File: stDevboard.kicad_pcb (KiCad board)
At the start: 4 copper layers, 50 x 50 mm, 73 parts, among them IC1 MPM3610GQV-Z, IC2 MMC5603NJ, IC3 ICM-42670-P, IC4 MAX-F10S-00B, IC5 ICM-45686, IC6 KTS1622EUAA-TR, J9 USB_C_Receptacle_USB2.0_16P, Q1 IRLML6402, Q10 IRLML6244, Q11 IRLML6402, Q12 IRLML6244, Q2 IRLML6244, Q3 IRLML6402, Q4 IRLML6244, Q5 IRLML6402, Q6 IRLML6244, Q7 IRLML6402, Q8 IRLML6244, Q9 IRLML6402, U1 STM32, U2 BMP581

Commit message: pcb coming along, schematic way more done - I now have a lot more respect for hardware people than I did earlier
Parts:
- added D2: D, Diode_SMD:D_0402_1005Metric, F.Cu at (35.5, 40.4)
- added J1: antenna, Connector_Coaxial:U.FL_Molex_MCRF_73412-0110_Vertical, F.Cu at (159.2, 128.1)
- added J8: battery, Connector_PinHeader_2.54mm:PinHeader_1x02_P2.54mm_Vertical, F.Cu at (161.8, 94.1)
- added R25: 100, Resistor_SMD:R_0805_2012Metric, F.Cu at (35.6, 34.7)
- C20, C21, C22: moved to B.Cu
- U1: value STM32 -> STM32U585CIUxQ
- moved IC6 136.5 mm to (21.9, 48.4)
- moved Q12 125.2 mm to (32.7, 27.6)
- moved Q6 125.2 mm to (22.8, 27.6)
- moved Q9 125.2 mm to (27.8, 27.6)
- moved Q1 125.2 mm to (17.9, 18.6)
- moved Q10 125.2 mm to (32.7, 18.6)
- moved Q11 125.2 mm to (32.7, 23.1)
- moved Q2 125.2 mm to (17.9, 23.1)
- moved Q3 125.2 mm to (17.9, 27.6)
- moved Q4 125.2 mm to (22.8, 18.6)
- moved Q5 125.2 mm to (22.8, 23.1)
- moved Q7 125.2 mm to (27.8, 18.6)
- moved Q8 125.2 mm to (27.8, 23.1)
- moved R10 122.1 mm to (18.0, 33.8)
- moved R11 122.1 mm to (18.0, 35.6)
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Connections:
- Q1 pad 3: Net-(J2-Pin_1) -> c1_test
- Q10 pad 3: Net-(J6-Pin_2) -> Net-(J2-Pin_2)
- Q11 pad 3: Net-(J7-Pin_1) -> c6_test
- Q12 pad 3: Net-(J7-Pin_2) -> Net-(J2-Pin_2)
- Q3 pad 3: Net-(J3-Pin_1) -> c2_test
- Q4 pad 3: Net-(J3-Pin_2) -> Net-(J2-Pin_2)
- Q5 pad 3: Net-(J4-Pin_1) -> c3_test
- Q6 pad 3: Net-(J4-Pin_2) -> Net-(J2-Pin_2)
- Q7 pad 3: Net-(J5-Pin_1) -> c4_test
- Q8 pad 3: Net-(J5-Pin_2) -> Net-(J2-Pin_2)
- Q9 pad 3: Net-(J6-Pin_1) -> c5_test
- U1 pad 18: unconnected-(U1-PB0-Pad18) -> c1_test
- U1 pad 19: unconnected-(U1-PB1-Pad19) -> c2_test
- U1 pad 37: unconnected-(U1-PA14-Pad37) -> cont_test
- U1 pad 39: unconnected-(U1-PB3-Pad39) -> c3_test
- U1 pad 40: unconnected-(U1-PB4-Pad40) -> c4_test
- U1 pad 41: unconnected-(U1-PB5-Pad41) -> c5_test
- U1 pad 42: unconnected-(U1-PB6-Pad42) -> c6_test
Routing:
- net +3.3V: track 0.00 -> 113.4 mm, vias 0 -> 17
- net GND: track 13.0 -> 126.0 mm, vias 0 -> 21
- net i2c1_sda: track 0.00 -> 50.0 mm, vias 0 -> 3
- net i2c1_sck: track 0.00 -> 49.3 mm, vias 0 -> 6
- net UART_MISO: track 0.00 -> 34.8 mm, vias 0 -> 2
- net RST: track 0.00 -> 33.6 mm, vias 0 -> 2
- net UART_MOSI: track 0.00 -> 32.8 mm, vias 0 -> 3
- net GPS_PULSE: track 0.00 -> 29.9 mm
- net USB_D-: track 0.00 -> 25.9 mm, vias 0 -> 2
- net USB_D+: track 0.00 -> 25.1 mm
- net bmp_int: track 0.00 -> 24.2 mm, vias 0 -> 2
- net lowrate_lowg_int2: track 0.00 -> 21.1 mm, vias 0 -> 3
- net Net-(C8-Pad1): track 4.33 -> 21.7 mm, vias 0 -> 2
- net highrate_highg_int1: track 0.00 -> 16.2 mm, vias 0 -> 2
- net Net-(J9-CC2): track 0.00 -> 13.9 mm, vias 0 -> 1
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- added copper zone on In2.Cu, net +3.3V
- added copper zone on B.Cu, net +5V
- added copper zone on F.Cu, net GND
- added copper zone on In1.Cu, net GND

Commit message: tons of progress on schematic and pcb - see journal for details
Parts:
- removed IC6: KTS1622EUAA-TR, footprints:KTS1622EUAA-TR
- removed J8: battery, Connector_PinHeader_2.54mm:PinHeader_1x02_P2.54mm_Vertical
- removed J9: USB_C_Receptacle_USB2.0_16P, Connector_USB:USB_C_Receptacle_GCT_USB4085
- removed Q10, Q12, Q8: IRLML6244, Package_TO_SOT_SMD:SOT-23
- removed Q11, Q7, Q9: IRLML6402, Package_TO_SOT_SMD:SOT-23
- added BOOT1: Conn_01x02, Connector_PinHeader_2.54mm:PinHeader_1x02_P2.54mm_Vertical, F.Cu at (52.9, 58.9)
- added BOOT2: Conn_01x02, Connector_PinHeader_2.54mm:PinHeader_1x02_P2.54mm_Vertical, F.Cu at (73.0, 58.9)
- added C27: 7.5pF, Capacitor_SMD:C_0402_1005Metric, F.Cu at (26.7, 66.3)
- added C28: 3.9pF, Capacitor_SMD:C_0402_1005Metric, F.Cu at (26.7, 68.2)
- added C29: 1.8pF, Capacitor_SMD:C_0402_1005Metric, F.Cu at (26.7, 70.2)
- added C30: 22pF, Capacitor_SMD:C_0402_1005Metric, F.Cu at (26.7, 72.2)
- added C31: 1.8pF, Capacitor_SMD:C_0402_1005Metric, F.Cu at (29.6, 64.3)
- added C32: 2.2pF, Capacitor_SMD:C_0402_1005Metric, F.Cu at (29.6, 66.3)
- added C33: 18pF, Capacitor_SMD:C_0402_1005Metric, F.Cu at (29.6, 68.2)
- added C34: 1uF, Capacitor_SMD:C_0603_1608Metric, F.Cu at (20.4, 55.4)
- added C35: 1uF, Capacitor_SMD:C_0603_1608Metric, F.Cu at (20.4, 57.9)
- added C36: 100nF, Capacitor_SMD:C_0402_1005Metric, F.Cu at (29.6, 70.2)
- added C37: 2.2uF, Capacitor_SMD:C_0603_1608Metric, F.Cu at (20.4, 60.4)
- added C38: 4.7uF, Capacitor_SMD:C_0603_1608Metric, F.Cu at (20.4, 62.9)
- added C39: 10uF, Capacitor_SMD:C_0603_1608Metric, F.Cu at (20.4, 65.4)
- added C40: 0.1uF, Capacitor_SMD:C_0402_1005Metric, F.Cu at (29.6, 72.2)
- added C41: 10uF, Capacitor_SMD:C_0603_1608Metric, F.Cu at (84.8, 57.9)
- added C42: 100nF, Capacitor_SMD:C_0402_1005Metric, F.Cu at (69.3, 48.3)
- added C43: 1uF, Capacitor_SMD:C_0603_1608Metric, F.Cu at (84.8, 60.4)
- added C44: 100nF, Capacitor_SMD:C_0402_1005Metric, F.Cu at (69.3, 50.3)
- added C45: 100nF, Capacitor_SMD:C_0402_1005Metric, F.Cu at (69.3, 52.2)
- added C46: 100nF, Capacitor_SMD:C_0402_1005Metric, F.Cu at (69.3, 54.2)
- added C47: 100nF, Capacitor_SMD:C_0402_1005Metric, F.Cu at (69.3, 56.2)
- added C48: 9pF, Capacitor_SMD:C_0402_1005Metric, F.Cu at (69.3, 58.2)
- added C49: 9pF, Capacitor_SMD:C_0402_1005Metric, F.Cu at (69.3, 60.1)
- added D3: D, Diode_SMD:D_0603_1608Metric, F.Cu at (29.3, 37.7)
- added D4: D_Schottky, Diode_SMD:D_0805_2012Metric, F.Cu at (133.3, 83.2)
- added FB1: BLM15AX102SN1D, footprints:NFZ15SG152SN10B, F.Cu at (123.8, 83.2)
- added FB2: BLM15AX102SN1D, footprints:NFZ15SG152SN10B, F.Cu at (126.2, 83.2)
- added J11: USB_C_Receptacle_USB2.0_16P, Connector_USB:USB_C_Receptacle_GCT_USB4085, F.Cu at (133.3, 81.0)
- added J12: Conn_01x06, Connector_PinHeader_2.54mm:PinHeader_1x06_P2.54mm_Vertical, F.Cu at (49.8, 91.2)
- added J2: USB_C_Receptacle_USB2.0_16P, Connector_USB:USB_C_Receptacle_GCT_USB4085, F.Cu at (122.7, 81.0)
- added J3: Conn_02x03_Top_Bottom, Connector_PinHeader_2.54mm:PinHeader_2x02_P2.54mm_Vertical, F.Cu at (92.7, 36.2)
- added L2: 12nH, Inductor_SMD:L_0402_1005Metric, F.Cu at (23.8, 52.6)
- added L3: 22nH, Inductor_SMD:L_0402_1005Metric, F.Cu at (23.8, 54.6)
- added L4: 4.7nH, Inductor_SMD:L_0402_1005Metric, F.Cu at (23.8, 56.6)
- added L5: 3.9nH, Inductor_SMD:L_0402_1005Metric, F.Cu at (23.8, 58.5)
- added L6: 7.5nH, Inductor_SMD:L_0402_1005Metric, F.Cu at (23.8, 60.5)
- added L7: 24nH, Inductor_SMD:L_0402_1005Metric, F.Cu at (23.8, 62.5)
- added L8: 2.2uH, Inductor_SMD:L_0402_1005Metric, F.Cu at (23.8, 64.5)
- added LR1: ~, footprints:Untitled, F.Cu at (31.8, 69.4)
- added R26: 10k, Resistor_SMD:R_0402_1005Metric, F.Cu at (81.4, 59.6)
- added R27: 10k, Resistor_SMD:R_0402_1005Metric, F.Cu at (81.4, 61.6)
- added R28: 10k, Resistor_SMD:R_0402_1005Metric, F.Cu at (81.4, 63.6)
- added RST1: Conn_01x02, Connector_PinHeader_2.54mm:PinHeader_1x02_P2.54mm_Vertical, F.Cu at (85.4, 92.6)
- added RST2: Conn_01x02, Connector_PinHeader_2.54mm:PinHeader_1x02_P2.54mm_Vertical, F.Cu at (77.6, 58.9)
- added U3: BMP581, footprints:BMP581, F.Cu at (125.0, 114.0)
- added U4: MAX-M10S, RF_GPS:ublox_MAX, F.Cu at (112.3, 159.6)
- added Y1: ECS-160-8-36B2-CKM-TR, footprints:ECS160836B2CKMTR, F.Cu at (106.2, 98.0)
- added Y2: CM7V-T1A-32.768KHZ, footprints:CM7V32768TBQA020, F.Cu at (105.2, 92.8)
- added Y3: ECS-TXO-25CSMV-320-AM-TR, footprints:ECSTXO25CSMV320AMTR, F.Cu at (34.0, 66.0)
- added Y4: CM7V-T1A-32.768KHZ, footprints:CM7V32768TBQA020, F.Cu at (83.7, 49.8)
- C1: value 22uF -> 10uF; footprint Capacitor_SMD:C_0603_1608Metric -> Capacitor_SMD:C_0805_2012Metric
- C10: value 1 uF -> 100 nF; footprint Capacitor_SMD:C_0603_1608Metric -> Capacitor_SMD:C_0402_1005Metric
- C12: value 10 uF -> 100 nF; footprint Capacitor_SMD:C_0603_1608Metric -> Capacitor_SMD:C_0402_1005Metric
- C13, C14: value 100 nF -> 2.2 uF; footprint Capacitor_SMD:C_0402_1005Metric -> Capacitor_SMD:C_0603_1608Metric
- C15: value 100 nF -> 1 uF; footprint Capacitor_SMD:C_0402_1005Metric -> Capacitor_SMD:C_0603_1608Metric
- C16: value 2.2uF -> 100 nF; footprint Capacitor_SMD:C_0603_1608Metric -> Capacitor_SMD:C_0402_1005Metric
- C17: value 0.1uF -> 10 uF; footprint Capacitor_SMD:C_0402_1005Metric -> Capacitor_SMD:C_0603_1608Metric; moved to B.Cu
- C18: value 10uF -> 100 nF; footprint Capacitor_SMD:C_0603_1608Metric -> Capacitor_SMD:C_0402_1005Metric; moved to B.Cu
- C19: value 0.1uf -> 100 nF
- C2: value 10uF -> 22uF
- C20: value 2.2uF -> 0.1uF; footprint Capacitor_SMD:C_0603_1608Metric -> Capacitor_SMD:C_0402_1005Metric; moved to F.Cu
- C21: moved to F.Cu
- C22: value 10nF -> 0.1uF; moved to F.Cu
- C23: value 10nF -> 0.1uF
- C24: value 2.2uF -> 10uF
- C25: value 0.1uF -> 2.2uF; footprint Capacitor_SMD:C_0402_1005Metric -> Capacitor_SMD:C_0603_1608Metric
- C26: value 100uF -> 47pF; footprint Capacitor_SMD:C_0805_2012Metric -> Capacitor_SMD:C_0402_1005Metric
- C3: value 10 uF -> 10uF
- C4: value 100 nF -> 8pF
- C5, C6: value 100 nF -> 9pF
- C7: value 1 uF -> 8pF; footprint Capacitor_SMD:C_0603_1608Metric -> Capacitor_SMD:C_0402_1005Metric
- C8: value 2.2 uF -> 1 uF
- C9: value 2.2 uF -> 10 uF
- D1: value D_Zener -> D; footprint Diode_SMD:D_0402_1005Metric -> Diode_SMD:D_0603_1608Metric
- D2: footprint Diode_SMD:D_0402_1005Metric -> Diode_SMD:D_0603_1608Metric
- IC2: value MMC5603NJ -> IRFR9014PBF; footprint footprints:MMC5603NJ -> footprints:TO228P990X238-3N
- IC3: value ICM-42670-P -> ICM-45686; moved to F.Cu
- IC4: value MAX-F10S-00B -> ICM-45686; footprint footprints:MAXF10S00B -> footprints:ICM42670P
- IC5: value ICM-45686 -> MMC5983MA; footprint footprints:ICM42670P -> footprints:MMC5983MA
- J1: value antenna -> battery; footprint Connector_Coaxial:U.FL_Molex_MCRF_73412-0110_Vertical -> Connector_PinHeader_2.54mm:PinHeader_1x02_P2.54mm_Vertical
- Q1, Q3, Q5: value IRLML6402 -> IRLML6244
- R1: value 100k -> 5.1K
- R10: value 100 -> 1k; footprint Resistor_SMD:R_0201_0603Metric -> Resistor_SMD:R_0402_1005Metric
- R11: value 100 -> 10k; footprint Resistor_SMD:R_0201_0603Metric -> Resistor_SMD:R_0402_1005Metric
- R12, R13: value 100 -> 2.7k; footprint Resistor_SMD:R_0201_0603Metric -> Resistor_SMD:R_0402_1005Metric
- R14: value 100 -> 1k; footprint Resistor_SMD:R_0201_0603Metric -> Resistor_SMD:R_0805_2012Metric
- R15: value 100 -> 10k; footprint Resistor_SMD:R_0201_0603Metric -> Resistor_SMD:R_0603_1608Metric
- R16, R17, R18, R19, R20, R21: footprint Resistor_SMD:R_0201_0603Metric -> Resistor_SMD:R_0603_1608Metric
- R22: value 39k -> 100; footprint Resistor_SMD:R_0201_0603Metric -> Resistor_SMD:R_0603_1608Metric
- R23: value 75k -> 5.1K; footprint Resistor_SMD:R_0201_0603Metric -> Resistor_SMD:R_0402_1005Metric
- R24: value 24k -> 5.1K; footprint Resistor_SMD:R_0201_0603Metric -> Resistor_SMD:R_0402_1005Metric
- R25: value 100 -> 1k; footprint Resistor_SMD:R_0805_2012Metric -> Resistor_SMD:R_0402_1005Metric
- R3: value 5.1K -> 75k; footprint Resistor_SMD:R_0402_1005Metric -> Resistor_SMD:R_0201_0603Metric
- R4: value 10k -> 24k; footprint Resistor_SMD:R_0402_1005Metric -> Resistor_SMD:R_0201_0603Metric
- R5: value 10k -> 39k; footprint Resistor_SMD:R_0402_1005Metric -> Resistor_SMD:R_0201_0603Metric
- R6: value 2.7k -> 100k
- R7, R8: value 2.7k -> 10k
- R9: value 2.7k -> 1k
- U1: value STM32U585CIUxQ -> STM32U073CCUx; footprint Package_DFN_QFN:QFN-48-1EP_7x7mm_P0.5mm_EP5.6x5.6mm -> Package_DFN_QFN:QFN-48-1EP_7x7mm_P0.5mm_EP5.6x5.6mm_ThermalVias
- U2: value BMP581 -> STM32U585CIUxQ; footprint footprints:BMP581 -> Package_DFN_QFN:QFN-48-1EP_7x7mm_P0.5mm_EP5.6x5.6mm_ThermalVias
- moved C25 164.9 mm to (20.4, 52.8)
- moved D1 160.9 mm to (29.3, 32.5), turned to 0 degrees
- moved R22 140.9 mm to (25.3, 41.7), turned to 0 degrees
- moved C9 137.1 mm to (48.6, 51.1), turned to 0 degrees
- moved R7 137.0 mm to (48.1, 63.4)
- moved R8 125.4 mm to (48.1, 65.4), turned to 0 degrees
- moved C23 125.3 mm to (77.5, 31.8)
- moved C22 125.0 mm to (77.5, 29.8), turned to 0 degrees
- moved C20 122.7 mm to (77.5, 25.8), turned to 0 degrees
- moved C21 120.7 mm to (77.5, 27.8), turned to 0 degrees
- moved C26 114.7 mm to (26.7, 64.3), turned to 0 degrees
- moved R10 111.3 mm to (110.1, 96.4)
- moved IC2 109.5 mm to (71.8, 71.0)
- moved C4 82.6 mm to (103.2, 97.9), turned to 90 degrees
- moved C8 78.0 mm to (108.8, 93.4), turned to -90 degrees
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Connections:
- C1 pad 1: GND -> +BATT
- C1 pad 2: +3.3V -> GND
- C12 pad 1: +3.3V -> GND
- C12 pad 2: GND -> +3.3V
- C13 pad 1: +3.3V -> Net-(C13-Pad1)
- C14 pad 1: GND -> Net-(C13-Pad1)
- C14 pad 2: Net-(D1-K) -> GND
- C19 pad 2: Net-(IC6-VDD_I2C) -> +3.3V
- C2 pad 1: +5V -> GND
- C2 pad 2: GND -> +3.3V
- C24 pad 1: +3.3V -> Net-(IC5-CAP)
- C25 pad 1: +3.3V -> GND
- C25 pad 2: GND -> +3.3V
- C26 pad 1: +5V -> vr_pa
- C3 pad 1: GND -> +BATT
- C3 pad 2: +3.3V -> GND
- C4 pad 1: GND -> Net-(Y1-OUT/IN)
- C4 pad 2: +3.3V -> Net-(Y1-GND_1)
- C5 pad 2: +3.3V -> Net-(C5-Pad2)
- C6 pad 1: GND -> Net-(U2-PC13)
- C6 pad 2: +3.3V -> GND
- C7 pad 1: GND -> Net-(U2-PH0)
- C7 pad 2: +3.3V -> Net-(Y1-GND_2)
- C8 pad 1: Net-(C8-Pad1) -> GND
- C9 pad 1: Net-(C8-Pad1) -> GND
- D1 pad 2: GND -> cont_test
- D2 pad 2: cont_test -> arm
- IC1 pad 16: +5V -> +BATT
- IC3 pad 4: lowrate_lowg_int1 -> imu1_int1
- IC3 pad 9: lowrate_lowg_int2 -> unconnected-(IC3-INT2-Pad9)
- IC4 pad 10: GND -> unconnected-(IC4-RESV_3-Pad10)
- IC4 pad 11: Net-(IC4-RF_IN) -> unconnected-(IC4-RESV_4-Pad11)
- IC4 pad 12: GND -> +3.3V
- IC4 pad 13: +3.3V -> i2c1_sck
- IC4 pad 14: +3.3V -> i2c1_sda
- IC4 pad 2: UART_MISO -> unconnected-(IC4-RESV_1-Pad2)
- IC4 pad 3: UART_MOSI -> unconnected-(IC4-RESV_2-Pad3)
- IC4 pad 4: GPS_PULSE -> imu2_int1
- IC4 pad 5: unconnected-(IC4-EXTINT-Pad5) -> +3.3V
- IC4 pad 6: +3.3V -> GND
- IC4 pad 7: +3.3V -> GND
- IC4 pad 9: RST -> unconnected-(IC4-INT2-Pad9)
- IC5 pad 1: +3.3V -> i2c1_sck
- IC5 pad 10: unconnected-(IC5-RESV_3-Pad10) -> Net-(IC5-CAP)
- IC5 pad 11: unconnected-(IC5-RESV_4-Pad11) -> GND
- IC5 pad 12: +3.3V -> unconnected-(IC5-NC_5-Pad12)
- IC5 pad 13: i2c1_sck -> +3.3V
- IC5 pad 14: i2c1_sda -> unconnected-(IC5-NC_6-Pad14)
- IC5 pad 2: unconnected-(IC5-RESV_1-Pad2) -> +3.3V
- IC5 pad 4: highrate_highg_int1 -> +3.3V
- IC5 pad 5: +3.3V -> unconnected-(IC5-SPI_SDO-Pad5)
- IC5 pad 6: GND -> unconnected-(IC5-NC_2-Pad6)
- IC5 pad 7: GND -> unconnected-(IC5-NC_3-Pad7)
- IC5 pad 8: +3.3V -> unconnected-(IC5-NC_4-Pad8)
- IC5 pad 9: highrate_highg_int2 -> GND
- J1 pad 1: Net-(IC4-RF_IN) -> GND
- J1 pad 2: GND -> +BATT
- L1 pad 1: Net-(U1-VLXSMPS) -> Net-(U2-VLXSMPS)
- L1 pad 2: Net-(C8-Pad1) -> Net-(C13-Pad1)
- Q1 pad 2: +5V -> GND
- Q1 pad 3: c1_test -> cont_test_out
- Q2 pad 3: Net-(J2-Pin_2) -> cont_test_out
- Q3 pad 2: +5V -> GND
- Q3 pad 3: c2_test -> cont_test_out
- Q4 pad 3: Net-(J2-Pin_2) -> cont_test_out
- Q5 pad 2: +5V -> GND
- Q5 pad 3: c3_test -> cont_test_out
- Q6 pad 3: Net-(J2-Pin_2) -> cont_test_out
- R1 pad 1: Net-(IC1-EN) -> Net-(J2-CC1)
- R1 pad 2: +5V -> GND
- R10 pad 1: Net-(Q2-G) -> Net-(C5-Pad2)
- R10 pad 2: c1_arm -> Net-(U2-PC14)
- R11 pad 1: Net-(Q1-G) -> Net-(RST1-Pin_2)
- R11 pad 2: c1_fire -> +3.3V
- R12 pad 1: Net-(Q3-G) -> i2c1_sda
- R12 pad 2: c2_fire -> +3.3V
- R13 pad 1: Net-(Q4-G) -> i2c1_sck
- R13 pad 2: c2_arm -> +3.3V
- R14 pad 1: Net-(Q5-G) -> cont_test_out
- R14 pad 2: c3_fire -> Net-(D1-K)
- R15 pad 1: Net-(Q6-G) -> Net-(D2-K)
- R15 pad 2: c3_arm -> +BATT
- R16 pad 1: Net-(Q7-G) -> Net-(Q1-G)
- R16 pad 2: c4_fire -> c1_fire
- R17 pad 1: Net-(Q8-G) -> cont_test_in
- R17 pad 2: c4_arm -> Net-(D3-K)
- R18 pad 1: Net-(Q9-G) -> Net-(Q2-G)
- R18 pad 2: c5_fire -> c2_fire
- R19 pad 1: Net-(Q10-G) -> Net-(Q3-G)
- R19 pad 2: c5_arm -> c3_fire
- R20 pad 1: Net-(Q11-G) -> Net-(Q4-G)
- R20 pad 2: c6_fire -> c4_fire
- R21 pad 1: Net-(Q12-G) -> Net-(Q5-G)
- R21 pad 2: c6_arm -> c5_fire
- R22 pad 1: Net-(IC1-AAM) -> Net-(Q6-G)
- R22 pad 2: GND -> c6_fire
- R23 pad 1: +3.3V -> Net-(J11-CC1)
- R23 pad 2: Net-(IC1-FB) -> GND
- R24 pad 1: Net-(IC1-FB) -> Net-(J11-CC2)
- R25 pad 1: Net-(J2-Pin_2) -> Net-(C48-Pad2)
- R25 pad 2: Net-(D2-K) -> Net-(U1-PC14)
- R3 pad 1: Net-(J9-CC2) -> +3.3V
- R3 pad 2: GND -> Net-(IC1-FB)
- R4 pad 1: Net-(BOOT1-Pad2) -> Net-(IC1-FB)
- R4 pad 2: Net-(U1-PH3) -> GND
- R5 pad 1: Net-(BOOT1-Pad2) -> Net-(IC1-AAM)
- R6 pad 1: Net-(IC2-SCL) -> Net-(IC1-EN)
- R6 pad 2: i2c1_sck -> +BATT
- R7 pad 1: Net-(IC2-SDA) -> GND
- R7 pad 2: i2c1_sda -> Net-(BOOT1-Pin_1)
- R8 pad 1: i2c1_sda -> Net-(BOOT1-Pin_1)
- R8 pad 2: +3.3V -> Net-(U2-PH3)
- R9 pad 1: i2c1_sck -> Net-(Y1-OUT/IN)
- R9 pad 2: +3.3V -> Net-(U2-PH1)
- U1 pad 10: UART_MOSI -> unconnected-(U1-PA0-Pad10)
- U1 pad 11: UART_MISO -> unconnected-(U1-PA1-Pad11)
- U1 pad 12: highrate_highg_int1 -> usart_mosi
- U1 pad 13: highrate_highg_int2 -> usart_miso
- U1 pad 14: lowrate_lowg_int1 -> usart_ck
- U1 pad 15: lowrate_lowg_int2 -> spi_sclk
- U1 pad 16: bmp_int -> spi_miso
- U1 pad 17: GPS_PULSE -> spi_mosi
- U1 pad 18: c1_test -> unconnected-(U1-PB0-Pad18)
- U1 pad 19: c2_test -> unconnected-(U1-PB1-Pad19)
- U1 pad 2: unconnected-(U1-PC13-Pad2) -> Net-(U1-PC13)
- U1 pad 20: Net-(U1-VLXSMPS) -> unconnected-(U1-PB2-Pad20)
- U1 pad 21: +3.3V -> unconnected-(U1-PB10-Pad21)
- U1 pad 22: GND -> unconnected-(U1-PB11-Pad22)
- U1 pad 23: Net-(C8-Pad1) -> GND
- U1 pad 24: GND -> +3.3V
- U1 pad 25: +3.3V -> unconnected-(U1-PB12-Pad25)
- U1 pad 3: unconnected-(U1-PC14-Pad3) -> Net-(U1-PC14)
- U1 pad 30: unconnected-(U1-PA9-Pad30) -> ppu_tx_external
- U1 pad 31: unconnected-(U1-PA10-Pad31) -> ppu_rx_external
- U1 pad 32: USB_D- -> USB2_D-
- U1 pad 33: USB_D+ -> USB2_D+
- U1 pad 37: cont_test -> telem_busy
- U1 pad 38: RST -> telem_rst
- U1 pad 39: c3_test -> unconnected-(U1-PB3-Pad39)
- U1 pad 40: c4_test -> unconnected-(U1-PB4-Pad40)
- U1 pad 41: c5_test -> unconnected-(U1-PB5-Pad41)
- U1 pad 42: c6_test -> unconnected-(U1-PB6-Pad42)
- U1 pad 43: i2c1_sda -> unconnected-(U1-PB7-Pad43)
- U1 pad 44: Net-(U1-PH3) -> Net-(U1-PF3)
- U1 pad 45: i2c1_sck -> unconnected-(U1-PB8-Pad45)
- U1 pad 46: Net-(C8-Pad1) -> unconnected-(U1-PB9-Pad46)
- U1 pad 7: Net-(D1-K) -> Net-(RST2-Pin_2)
- U2 pad 10: +3.3V -> /main micro/servo1
- U2 pad 2: i2c1_sck -> Net-(U2-PC13)
- U2 pad 3: GND -> Net-(U2-PC14)
- U2 pad 4: i2c1_sda -> unconnected-(U2-PC15-Pad4)
- U2 pad 5: GND -> Net-(U2-PH0)
- U2 pad 6: +3.3V -> Net-(U2-PH1)
- U2 pad 7: bmp_int -> Net-(RST1-Pin_2)
- U2 pad 9: GND -> +3.3V
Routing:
- net +3.3V: track 113.4 -> 43.6 mm, vias 17 -> 27
- net i2c1_sda: track 50.0 -> 0.00 mm, vias 3 -> 0
- net i2c1_sck: track 49.3 -> 5.55 mm, vias 6 -> 0
- net UART_MISO: track 34.8 -> 0.00 mm, vias 2 -> 0
- net RST: track 33.6 -> 0.00 mm, vias 2 -> 0
- net UART_MOSI: track 32.8 -> 0.00 mm, vias 3 -> 0
- net +BATT: track 0.00 -> 30.8 mm
- net GPS_PULSE: track 29.9 -> 0.00 mm
- net Net-(C13-Pad1): track 0.00 -> 26.4 mm, vias 0 -> 1
- net Net-(C8-Pad1): track 21.7 -> 0.00 mm, vias 2 -> 0
- net lowrate_lowg_int2: track 21.1 -> 0.00 mm, vias 3 -> 0
- net Net-(J2-SHIELD): track 0.00 -> 18.8 mm
- net Net-(J11-SHIELD): track 0.00 -> 18.8 mm
- net highrate_highg_int1: track 16.2 -> 0.00 mm, vias 2 -> 0
- net USB2_D-: track 0.00 -> 14.0 mm, vias 0 -> 1
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- added copper zone on In1.Cu, net +3.3V
- added copper zone on B.Cu, net GND
- added copper zone on In2.Cu, net GND
- removed copper zone on In2.Cu, net +3.3V
- removed copper zone on B.Cu, net +5V
- removed copper zone on In1.Cu, net GND
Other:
- board size 50 x 50 mm -> 50 x 100 mm

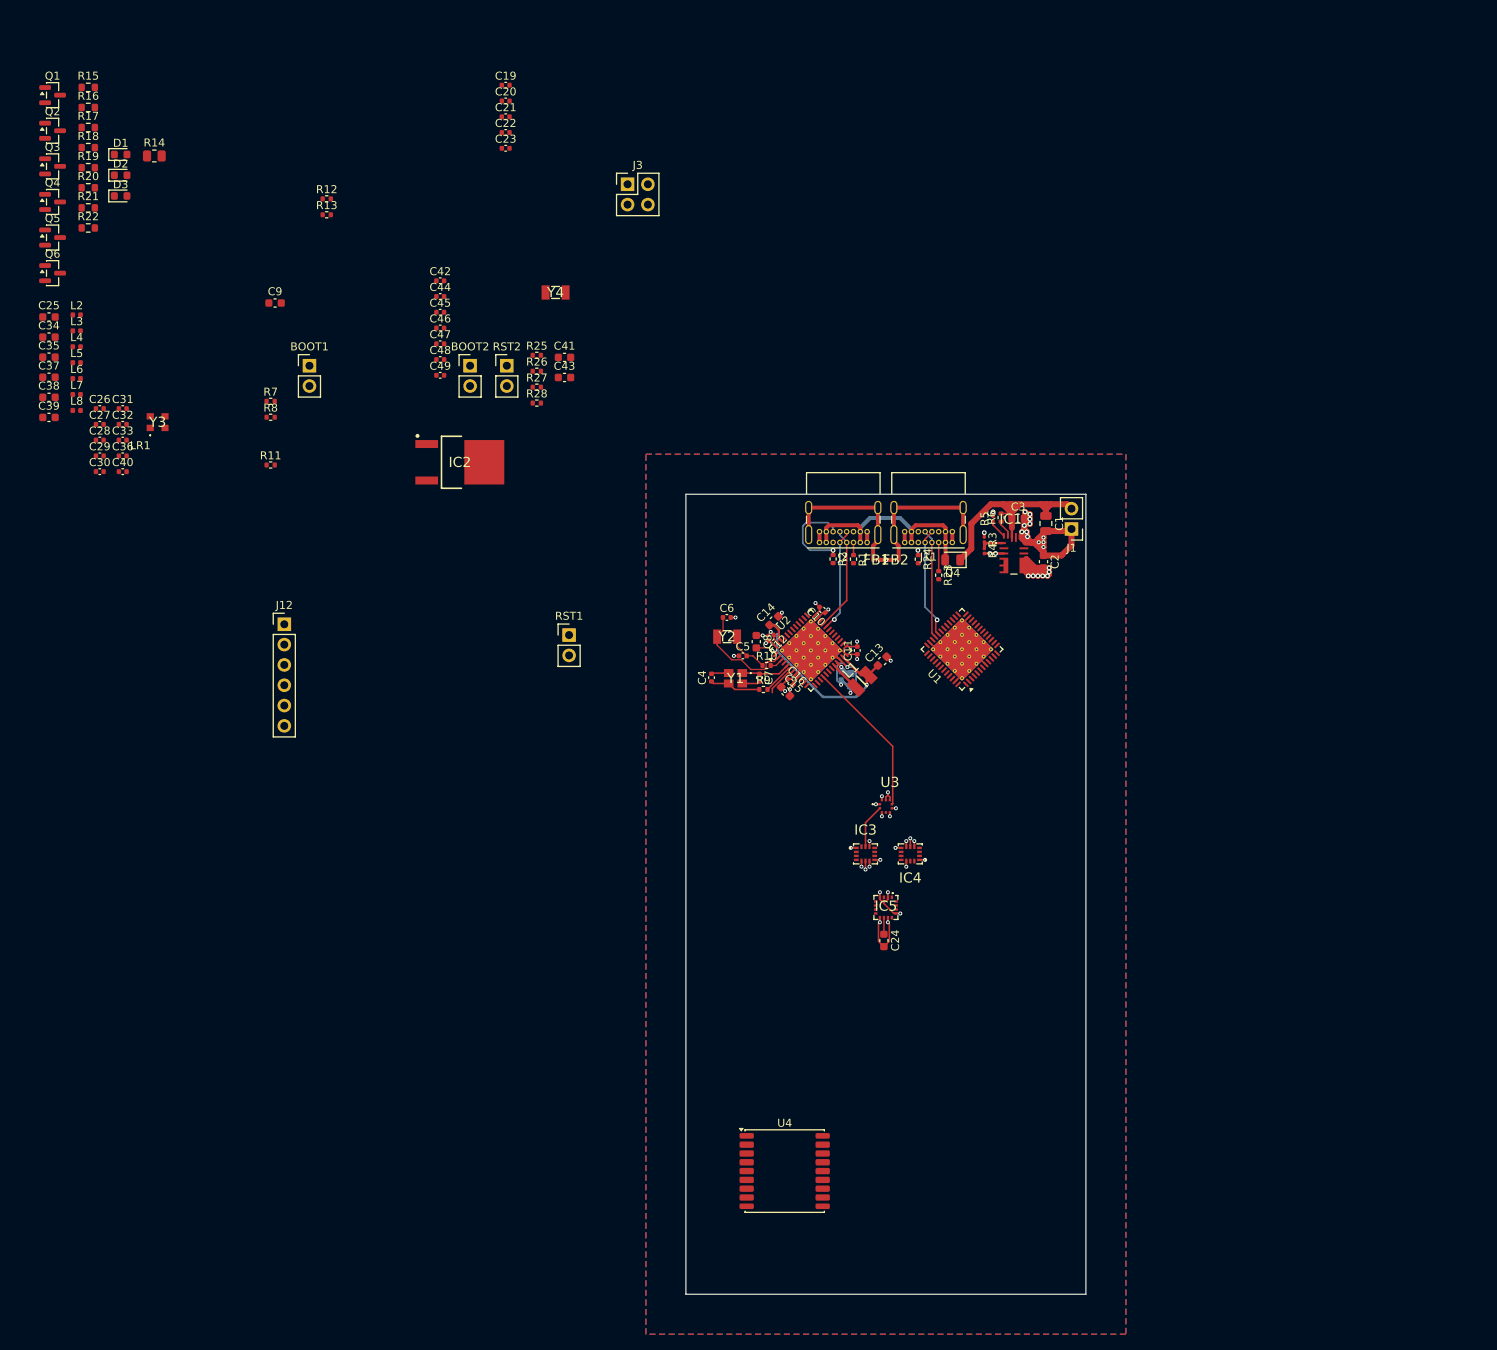
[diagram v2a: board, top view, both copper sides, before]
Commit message: added mounting holes, moved power stuff, routed secondary micro, moved sensors
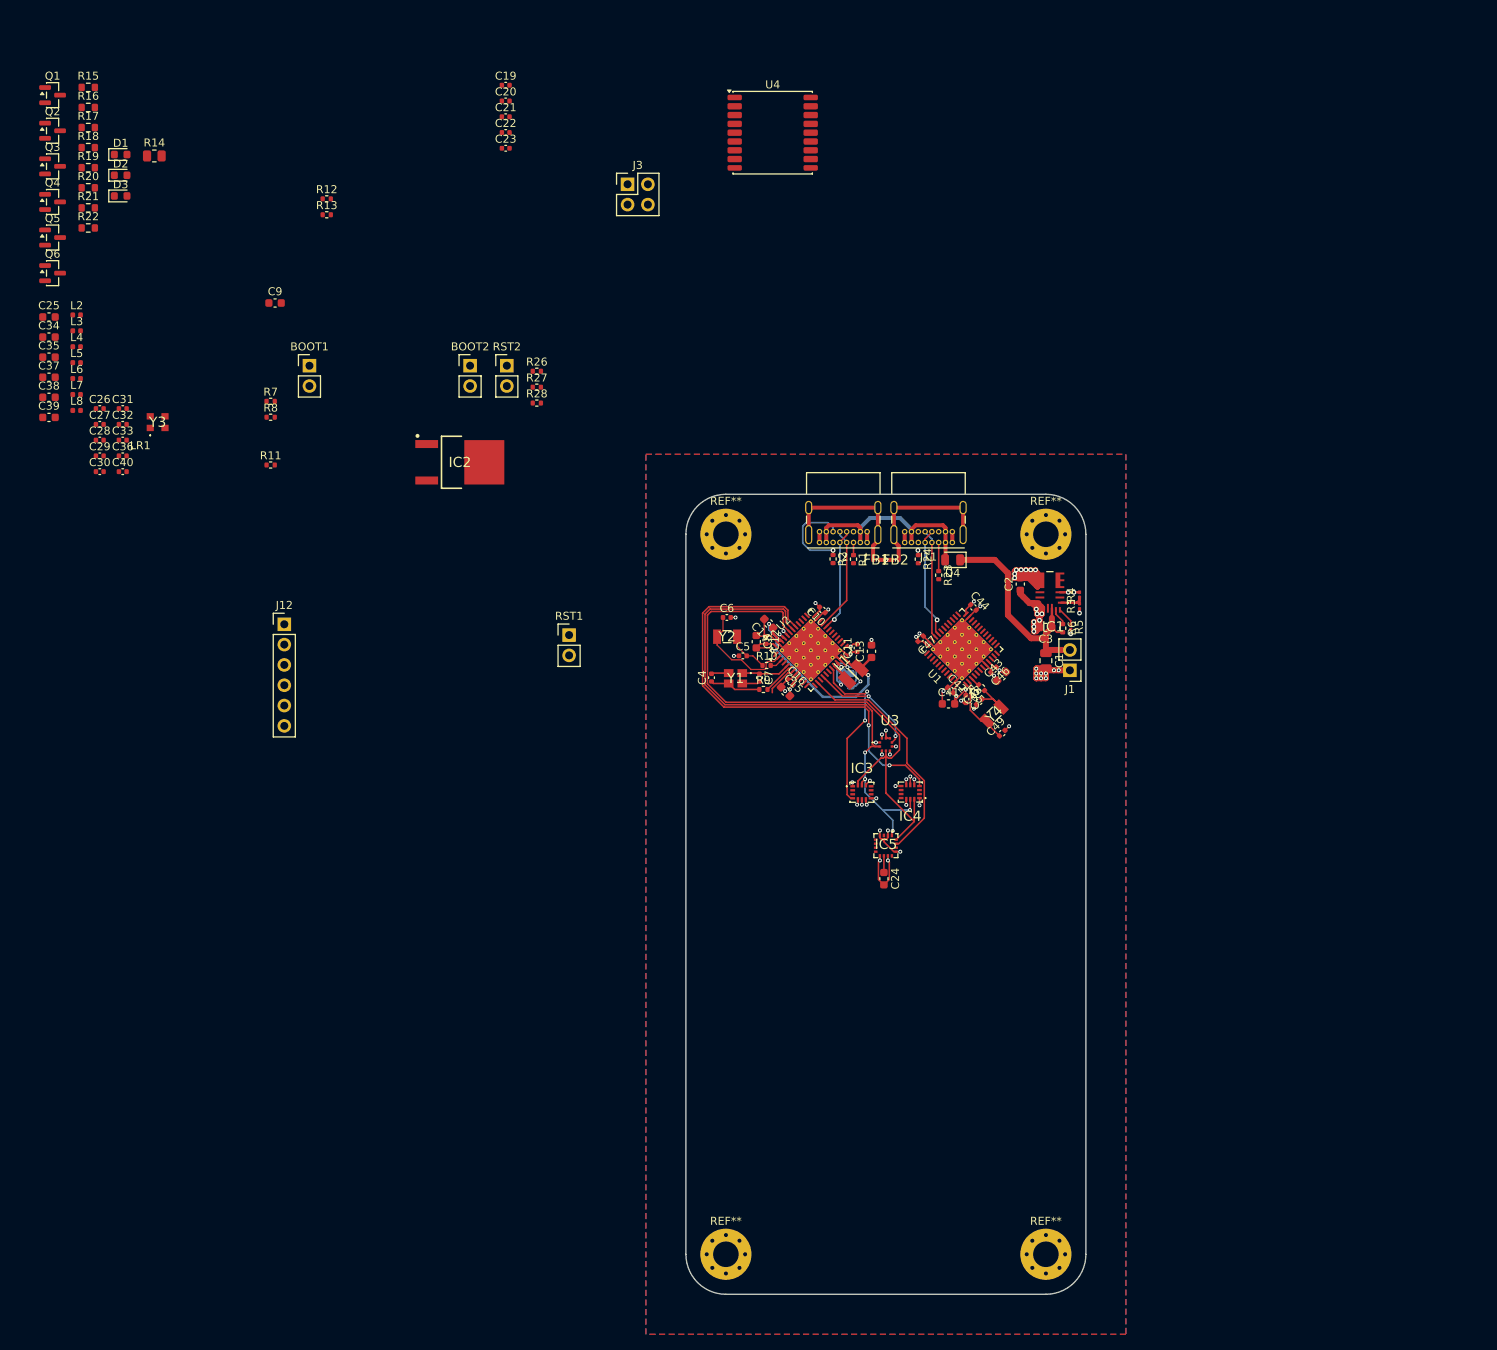
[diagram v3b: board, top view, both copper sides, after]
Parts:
- added REF**: MountingHole_3.2mm_M3_Pad_Via, MountingHole:MountingHole_3.2mm_M3_Pad_Via, F.Cu at (145.0, 80.0)
- added REF**: MountingHole_3.2mm_M3_Pad_Via, MountingHole:MountingHole_3.2mm_M3_Pad_Via, F.Cu at (105.0, 170.0)
- added REF**: MountingHole_3.2mm_M3_Pad_Via, MountingHole:MountingHole_3.2mm_M3_Pad_Via, F.Cu at (105.0, 80.0)
- added REF**: MountingHole_3.2mm_M3_Pad_Via, MountingHole:MountingHole_3.2mm_M3_Pad_Via, F.Cu at (145.0, 170.0)
- moved U4 129.8 mm to (110.8, 29.8)
- moved C49 83.3 mm to (139.5, 104.9), turned to 45 degrees
- moved C42 81.7 mm to (133.1, 99.5), turned to -45 degrees
- moved C45 81.6 mm to (135.0, 100.6), turned to -90 degrees
- moved C46 81.3 mm to (138.5, 96.9), turned to -135 degrees
- moved C48 79.8 mm to (136.7, 100.9), turned to 45 degrees
- moved C44 77.1 mm to (135.9, 89.1), turned to -45 degrees
- moved Y4 76.0 mm to (138.5, 102.5), turned to 45 degrees
- moved C47 70.5 mm to (129.3, 93.1), turned to -135 degrees
- moved R25 69.4 mm to (137.0, 99.2), turned to 135 degrees
- moved C43 66.2 mm to (139.5, 97.7), turned to 45 degrees
- moved C41 64.7 mm to (132.8, 101.2)
- moved J1 17.7 mm to (148.0, 97.0)
- moved C1 17.1 mm to (145.0, 95.8)
- moved R5 16.7 mm to (148.1, 91.6), turned to -90 degrees
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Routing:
- net i2c1_sda: track 0.00 -> 73.5 mm
- net i2c1_sck: track 5.55 -> 69.1 mm, vias 0 -> 4
- net imu2_int1: track 0.00 -> 58.5 mm, vias 0 -> 2
- net mag_int: track 0.00 -> 29.8 mm
- net imu1_int1: track 0.00 -> 21.6 mm, vias 0 -> 2
- net +3.3V: track 43.6 -> 57.4 mm, vias 27 -> 31
- net Net-(U1-PC13): track 0.00 -> 8.83 mm
- net GND: track 121.9 -> 128.6 mm, vias 38 -> 46
- net Net-(C48-Pad2): track 0.00 -> 5.75 mm
- net bmp_int: track 19.6 -> 14.0 mm, vias 0 -> 2
- net +BATT: track 30.8 -> 28.5 mm
- net Net-(C13-Pad1): track 26.4 -> 28.4 mm, vias 1 -> 2
- net Net-(U2-VLXSMPS): track 3.84 -> 2.49 mm
- net Net-(U1-PC14): track 0.00 -> 1.21 mm
- net gps_int: track 0.00 -> 0.80 mm, vias 0 -> 1
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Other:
- outline, holes or cut-outs redrawn

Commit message: worked mainly on pcb
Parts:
- added C50: C, Capacitor_SMD:C_0402_1005Metric, F.Cu at (132.2, 165.4)
- added C51: C, Capacitor_SMD:C_0402_1005Metric, F.Cu at (132.2, 168.4)
- added J10: 73412-0114, footprints:73412-0110, F.Cu at (115.0, 171.0)
- added J13: Conn_01x04, Connector_PinHeader_2.54mm:PinHeader_1x04_P2.54mm_Vertical, F.Cu at (102.0, 101.9)
- added L9: L, Inductor_SMD:L_0402_1005Metric, F.Cu at (131.7, 166.9)
- C20, C21, C22, C23, C40: value 0.1uF -> 100nF
- J12: value Conn_01x06 -> 73412-0114; footprint Connector_PinHeader_2.54mm:PinHeader_1x06_P2.54mm_Vertical -> footprints:73412-0110
- J3: footprint Connector_PinHeader_2.54mm:PinHeader_2x02_P2.54mm_Vertical -> Connector_PinHeader_2.54mm:PinHeader_2x03_P2.54mm_Vertical
- L2: footprint Inductor_SMD:L_0402_1005Metric -> Inductor_SMD:L_0603_1608Metric
- L8: footprint Inductor_SMD:L_0402_1005Metric -> Inductor_SMD:L_0805_2012Metric
- LR1: footprint footprints:Untitled -> footprints:LR2021
- moved C25 141.1 mm to (120.0, 152.8), turned to 180 degrees
- moved L2 135.3 mm to (113.2, 154.1)
- moved C34 132.4 mm to (110.2, 152.6), turned to 180 degrees
- moved U4 130.5 mm to (135.0, 158.0), turned to -90 degrees
- moved C35 130.4 mm to (117.2, 145.2), turned to 90 degrees
- moved L7 129.4 mm to (115.2, 154.1), turned to -90 degrees
- moved C37 127.6 mm to (115.7, 145.2), turned to 90 degrees
- moved C32 124.1 mm to (115.7, 155.6)
- moved C38 123.4 mm to (110.3, 147.4), turned to 180 degrees
- moved C33 123.3 mm to (115.2, 156.9), turned to -90 degrees
- moved L8 120.8 mm to (113.2, 145.8), turned to 180 degrees
- moved Y3 120.5 mm to (120.7, 149.7), turned to -90 degrees
- moved LR1 115.8 mm to (115.0, 150.0), turned to 180 degrees
- moved J12 114.3 mm to (131.7, 171.0), turned to 180 degrees
- moved C36 113.0 mm to (110.9, 148.7), turned to 180 degrees
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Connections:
- D3 pad 2: unconnected-(D3-A-Pad2) -> /mosfets/sense pin
- J12 pad 1: +BATT -> Net-(J12-SIGNAL)
- J12 pad 2: /main micro/servo1 -> GND
- J12 pad 3: /main micro/servo2 -> GND
- J12 pad 4: /main micro/servo3 -> GND
- J3 pad 1: mpu_tx_external -> GND
- J3 pad 2: mpu_rx_external -> +3.3V
- J3 pad 3: GND -> ppu_tx_external
- J3 pad 4: ppu_tx_external -> mpu_tx_external
- U4 pad 11: unconnected-(U4-RF_IN-Pad11) -> Net-(U4-RF_IN)
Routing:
- net GND: track 128.6 -> 171.3 mm, vias 46 -> 100
- net usart_mosi: track 0.00 -> 32.2 mm, vias 0 -> 2
- net usart_miso: track 0.00 -> 29.6 mm, vias 0 -> 2
- net +3.3V: track 57.4 -> 84.7 mm, vias 31 -> 45
- net usart_ck: track 0.00 -> 26.6 mm, vias 0 -> 2
- net /main micro/servo4: track 0.00 -> 18.8 mm, vias 0 -> 1
- net /main micro/servo3: track 0.00 -> 16.9 mm, vias 0 -> 1
- net /main micro/servo2: track 0.00 -> 15.6 mm, vias 0 -> 1
- net Net-(RST1-Pin_2): track 3.98 -> 18.8 mm, vias 0 -> 1
- net /main micro/servo1: track 0.00 -> 14.2 mm, vias 0 -> 1
- net i2c1_sck: track 69.1 -> 83.1 mm
- net i2c1_sda: track 73.5 -> 86.8 mm
- net Net-(RST2-Pin_2): track 0.00 -> 13.1 mm, vias 0 -> 1
- net mpu_rx_external: track 0.00 -> 11.7 mm
- net ppu_tx_external: track 0.00 -> 9.56 mm, vias 0 -> 1
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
